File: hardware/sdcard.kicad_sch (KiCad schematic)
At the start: 18 parts

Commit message: train schematics
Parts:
- C?: value 1u -> 4.7u; Voltage 6.3V -> 15V
- C?: Voltage 10V -> 50V
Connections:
- net VDD_SYS_3V3 renamed VDD_AUX_3V3
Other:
- company: Erdapfel -> Frisius
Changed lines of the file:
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@@
     (date "2021-12-17")
     (rev "A")
-    (company "Erdapfel")
+    (company "Frisius")
   )
   (junction (at 109.22 72.39) (diameter 0) (color 0 0 0 0)
@@
       (effects (font (size 0.8 0.8)) (justify left))
     )
-    (property "Value" "1u" (id 1) (at 82.55 45.72 0)
+    (property "Value" "4.7u" (id 1) (at 82.55 45.72 0)
       (effects (font (size 0.8 0.8)) (justify left))
     )
@@
       (effects (font (size 0.8 0.8)) hide)
     )
-    (property "Voltage" "6.3V" (id 4) (at 82.55 46.99 0)
-      (effects (font (size 0.8 0.8)) (justify left))
-    )
-    (pin "1")
-    (pin "2")
+    (property "Voltage" "15V" (id 4) (at 82.55 46.99 0)
+      (effects (font (size 0.8 0.8)) (justify left))
+    )
+    (pin "1")
+    (pin "2")
+  )
+  (symbol (lib_id "bt_power:VDD_AUX_3V3") (at 72.39 40.64 0) (unit 1)
+    (in_bom no) (on_board no)
+    (property "Reference" "U?" (id 0) (at 72.9234 40.64 0)
+      (effects (font (size 1.27 1.27)) hide)
+    )
+    (property "Value" "VDD_AUX_3V3" (id 1) (at 66.04 36.83 0)
+      (effects (font (size 1.27 1.27)) (justify left))
+    )
+    (property "Footprint" "" (id 2) (at 72.9234 40.64 0)
+      (effects (font (size 1.27 1.27)) hide)
+    )
+    (property "Datasheet" "" (id 3) (at 72.9234 40.64 0)
+      (effects (font (size 1.27 1.27)) hide)
+    )
+    (pin "1")
   )
   (symbol (lib_id "Device:R_Small") (at 99.06 45.72 180) (unit 1)
@@
     (pin "2")
   )
-  (symbol (lib_id "bt_power:VDD_SYS_3V3") (at 72.39 40.64 0) (mirror y) (unit 1)
-    (in_bom no) (on_board no)
-    (property "Reference" "U?" (id 0) (at 71.8566 40.64 0)
-      (effects (font (size 0.8 0.8)) hide)
-    )
-    (property "Value" "VDD_SYS_3V3" (id 1) (at 72.39 36.83 0)
-      (effects (font (size 0.8 0.8)))
-    )
-    (property "Footprint" "" (id 2) (at 71.8566 40.64 0)
-      (effects (font (size 0.8 0.8)) hide)
-    )
-    (property "Datasheet" "" (id 3) (at 71.8566 40.64 0)
-      (effects (font (size 0.8 0.8)) hide)
-    )
-    (pin "1")
-  )
   (symbol (lib_id "Device:R_Small") (at 93.98 45.72 180) (unit 1)
     (in_bom yes) (on_board yes)
@@
       (effects (font (size 0.8 0.8)) hide)
     )
-    (property "Voltage" "10V" (id 4) (at 74.93 46.99 0)
-      (effects (font (size 0.8 0.8)) (justify left))
-    )
+    (property "Voltage" "50V" (id 4) (at 74.93 46.99 0)
+      (effects (font (size 0.8 0.8)) (justify left))
+    )

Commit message: ready for first review
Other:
- moved on the sheet: C?, J?, R?

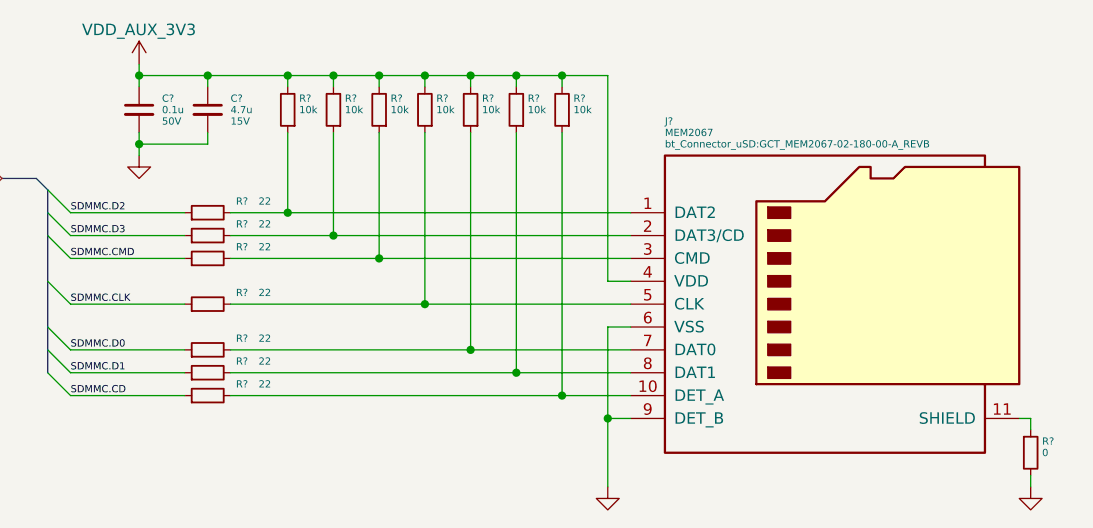
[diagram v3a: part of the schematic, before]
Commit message: checking footprint assignment, added current sense pac1934 for dev
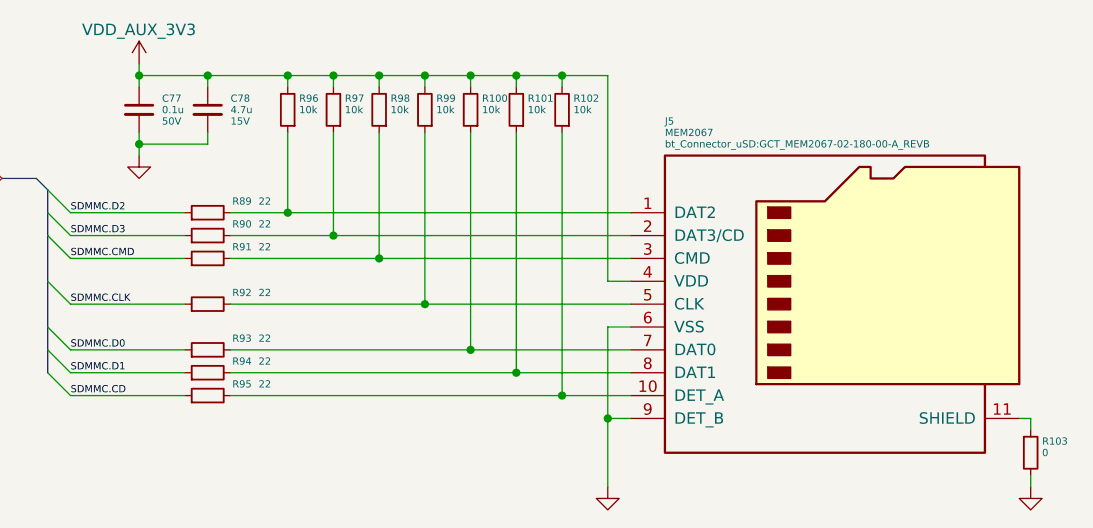
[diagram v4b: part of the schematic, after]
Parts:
- gave numbers to parts that had none: 18
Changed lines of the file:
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@@
   (symbol (lib_id "Device:R_Small") (at 111.76 90.17 90) (unit 1)
     (in_bom yes) (on_board yes)
-    (property "Reference" "R?" (id 0) (at 115.57 88.9 90)
+    (property "Reference" "R89" (id 0) (at 115.57 88.9 90)
       (effects (font (size 0.8 0.8)))
     )
@@
   (symbol (lib_id "Device:R_Small") (at 111.76 110.49 90) (unit 1)
     (in_bom yes) (on_board yes)
-    (property "Reference" "R?" (id 0) (at 115.57 109.22 90)
+    (property "Reference" "R95" (id 0) (at 115.57 109.22 90)
       (effects (font (size 0.8 0.8)))
     )
@@
   (symbol (lib_id "Device:R_Small") (at 120.65 78.74 180) (unit 1)
     (in_bom yes) (on_board yes)
-    (property "Reference" "R?" (id 0) (at 121.92 77.47 0)
+    (property "Reference" "R96" (id 0) (at 121.92 77.47 0)
       (effects (font (size 0.8 0.8)) (justify right))
     )
@@
   (symbol (lib_id "Device:C_Small") (at 111.76 78.74 0) (unit 1)
     (in_bom yes) (on_board yes)
-    (property "Reference" "C?" (id 0) (at 114.3 77.47 0)
+    (property "Reference" "C78" (id 0) (at 114.3 77.47 0)
       (effects (font (size 0.8 0.8)) (justify left))
     )
@@
   (symbol (lib_id "bt_power:VDD_AUX_3V3") (at 104.14 73.66 0) (unit 1)
     (in_bom no) (on_board no)
-    (property "Reference" "U?" (id 0) (at 104.6734 73.66 0)
+    (property "Reference" "#U046" (id 0) (at 104.6734 73.66 0)
       (effects (font (size 1.27 1.27)) hide)
     )
@@
   (symbol (lib_id "Device:R_Small") (at 130.81 78.74 180) (unit 1)
     (in_bom yes) (on_board yes)
-    (property "Reference" "R?" (id 0) (at 132.08 77.47 0)
+    (property "Reference" "R98" (id 0) (at 132.08 77.47 0)
       (effects (font (size 0.8 0.8)) (justify right))
     )
@@
   (symbol (lib_id "Device:R_Small") (at 203.2 116.84 0) (unit 1)
     (in_bom no) (on_board yes)
-    (property "Reference" "R?" (id 0) (at 204.47 115.57 0)
+    (property "Reference" "R103" (id 0) (at 204.47 115.57 0)
       (effects (font (size 0.8 0.8)) (justify left))
     )
@@
   (symbol (lib_id "power:GND") (at 156.21 120.65 0) (unit 1)
     (in_bom yes) (on_board yes)
-    (property "Reference" "#PWR?" (id 0) (at 156.21 127 0)
+    (property "Reference" "#PWR081" (id 0) (at 156.21 127 0)
       (effects (font (size 0.8 0.8)) hide)
     )
@@
   (symbol (lib_id "Device:R_Small") (at 111.76 92.71 90) (unit 1)
     (in_bom yes) (on_board yes)
-    (property "Reference" "R?" (id 0) (at 115.57 91.44 90)
+    (property "Reference" "R90" (id 0) (at 115.57 91.44 90)
       (effects (font (size 0.8 0.8)))
     )
@@
   (symbol (lib_id "Device:R_Small") (at 125.73 78.74 180) (unit 1)
     (in_bom yes) (on_board yes)
-    (property "Reference" "R?" (id 0) (at 127 77.47 0)
+    (property "Reference" "R97" (id 0) (at 127 77.47 0)
       (effects (font (size 0.8 0.8)) (justify right))
     )
@@
   (symbol (lib_id "Device:R_Small") (at 111.76 105.41 90) (unit 1)
     (in_bom yes) (on_board yes)
-    (property "Reference" "R?" (id 0) (at 115.57 104.14 90)
+    (property "Reference" "R93" (id 0) (at 115.57 104.14 90)
       (effects (font (size 0.8 0.8)))
     )
@@
   (symbol (lib_id "Device:R_Small") (at 111.76 95.25 90) (unit 1)
     (in_bom yes) (on_board yes)
-    (property "Reference" "R?" (id 0) (at 115.57 93.98 90)
+    (property "Reference" "R91" (id 0) (at 115.57 93.98 90)
       (effects (font (size 0.8 0.8)))
     )
@@
   (symbol (lib_id "Device:R_Small") (at 146.05 78.74 180) (unit 1)
     (in_bom yes) (on_board yes)
-    (property "Reference" "R?" (id 0) (at 147.32 77.47 0)
+    (property "Reference" "R101" (id 0) (at 147.32 77.47 0)
       (effects (font (size 0.8 0.8)) (justify right))
     )
@@
   (symbol (lib_id "Device:R_Small") (at 111.76 100.33 90) (unit 1)
     (in_bom yes) (on_board yes)
-    (property "Reference" "R?" (id 0) (at 115.57 99.06 90)
+    (property "Reference" "R92" (id 0) (at 115.57 99.06 90)
       (effects (font (size 0.8 0.8)))
     )
@@
   (symbol (lib_id "Device:R_Small") (at 135.89 78.74 180) (unit 1)
     (in_bom yes) (on_board yes)
-    (property "Reference" "R?" (id 0) (at 137.16 77.47 0)
+    (property "Reference" "R99" (id 0) (at 137.16 77.47 0)
       (effects (font (size 0.8 0.8)) (justify right))
     )
@@
   (symbol (lib_id "power:GND") (at 104.14 83.82 0) (mirror y) (unit 1)
     (in_bom yes) (on_board yes)
-    (property "Reference" "#PWR?" (id 0) (at 104.14 90.17 0)
+    (property "Reference" "#PWR080" (id 0) (at 104.14 90.17 0)
       (effects (font (size 0.8 0.8)) hide)
     )
@@
   (symbol (lib_id "Device:R_Small") (at 111.76 107.95 90) (unit 1)
     (in_bom yes) (on_board yes)
-    (property "Reference" "R?" (id 0) (at 115.57 106.68 90)
+    (property "Reference" "R94" (id 0) (at 115.57 106.68 90)
       (effects (font (size 0.8 0.8)))
     )
@@
   (symbol (lib_id "power:GND") (at 203.2 120.65 0) (unit 1)
     (in_bom yes) (on_board yes)
-    (property "Reference" "#PWR?" (id 0) (at 203.2 127 0)
+    (property "Reference" "#PWR082" (id 0) (at 203.2 127 0)
       (effects (font (size 0.8 0.8)) hide)
     )
@@
   (symbol (lib_id "Device:R_Small") (at 140.97 78.74 180) (unit 1)
     (in_bom yes) (on_board yes)
-    (property "Reference" "R?" (id 0) (at 142.24 77.47 0)
+    (property "Reference" "R100" (id 0) (at 142.24 77.47 0)
       (effects (font (size 0.8 0.8)) (justify right))
     )
@@
   (symbol (lib_id "Device:R_Small") (at 151.13 78.74 180) (unit 1)
     (in_bom yes) (on_board yes)
-    (property "Reference" "R?" (id 0) (at 152.4 77.47 0)
+    (property "Reference" "R102" (id 0) (at 152.4 77.47 0)
       (effects (font (size 0.8 0.8)) (justify right))
     )
@@
   (symbol (lib_id "Device:C_Small") (at 104.14 78.74 0) (unit 1)
     (in_bom yes) (on_board yes)
-    (property "Reference" "C?" (id 0) (at 106.68 77.47 0)
+    (property "Reference" "C77" (id 0) (at 106.68 77.47 0)
       (effects (font (size 0.8 0.8)) (justify left))
     )
@@
   (symbol (lib_id "Connector:Micro_SD_Card_Det") (at 181.61 100.33 0) (unit 1)
     (in_bom yes) (on_board yes)
-    (property "Reference" "J?" (id 0) (at 162.56 80.01 0)
-      (effects (font (size 0.8 0.8)) (justify left))
-    )
+    (property "Reference" "J5" (id 0) (at 162.56 80.01 0)
+      (effects (font (size 0.8 0.8)) (justify left))
+    )

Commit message: hardware update
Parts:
- removed R103: 0, Resistor_SMD:R_0603_1608Metric, symbol Device:R_Small
- R45: renamed from R89; footprint Resistor_SMD:R_0603_1608Metric -> Resistor_SMD:R_0402_1005Metric
- R46: renamed from R90; footprint Resistor_SMD:R_0603_1608Metric -> Resistor_SMD:R_0402_1005Metric
- R47: renamed from R91; footprint Resistor_SMD:R_0603_1608Metric -> Resistor_SMD:R_0402_1005Metric
- R48: renamed from R92; footprint Resistor_SMD:R_0603_1608Metric -> Resistor_SMD:R_0402_1005Metric
- R49: renamed from R93; footprint Resistor_SMD:R_0603_1608Metric -> Resistor_SMD:R_0402_1005Metric
- R50: renamed from R94; footprint Resistor_SMD:R_0603_1608Metric -> Resistor_SMD:R_0402_1005Metric
- R51: renamed from R95; footprint Resistor_SMD:R_0603_1608Metric -> Resistor_SMD:R_0402_1005Metric
- R52: renamed from R96; footprint Resistor_SMD:R_0603_1608Metric -> Resistor_SMD:R_0402_1005Metric
- R53: renamed from R97; footprint Resistor_SMD:R_0603_1608Metric -> Resistor_SMD:R_0402_1005Metric
- R54: renamed from R98; footprint Resistor_SMD:R_0603_1608Metric -> Resistor_SMD:R_0402_1005Metric
- R55: renamed from R99; footprint Resistor_SMD:R_0603_1608Metric -> Resistor_SMD:R_0402_1005Metric
- R56: renamed from R100; footprint Resistor_SMD:R_0603_1608Metric -> Resistor_SMD:R_0402_1005Metric
- R57: renamed from R101; footprint Resistor_SMD:R_0603_1608Metric -> Resistor_SMD:R_0402_1005Metric
- R58: renamed from R102; footprint Resistor_SMD:R_0603_1608Metric -> Resistor_SMD:R_0402_1005Metric
- renumbered C77 to C53, C78 to C54, J5 to J4
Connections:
- net GND: now also J4.11 (SHIELD)

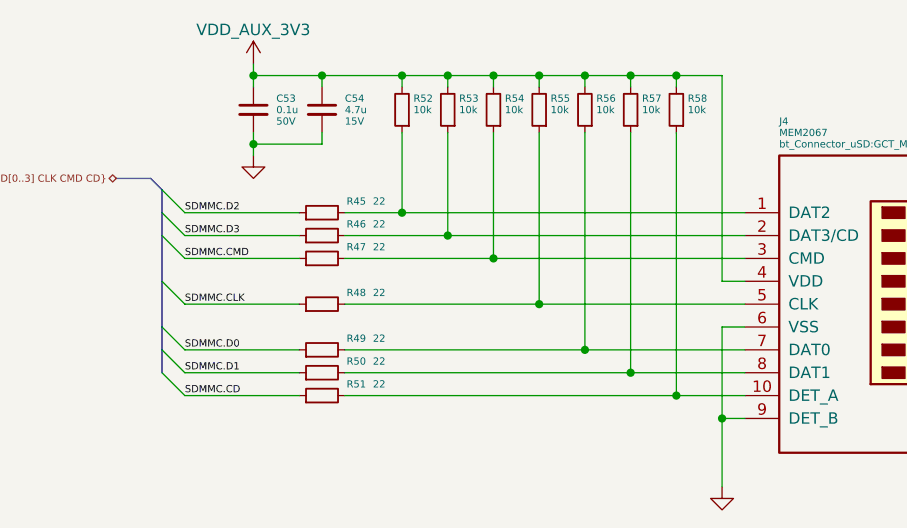
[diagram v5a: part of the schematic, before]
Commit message: initial component placement and design simplification
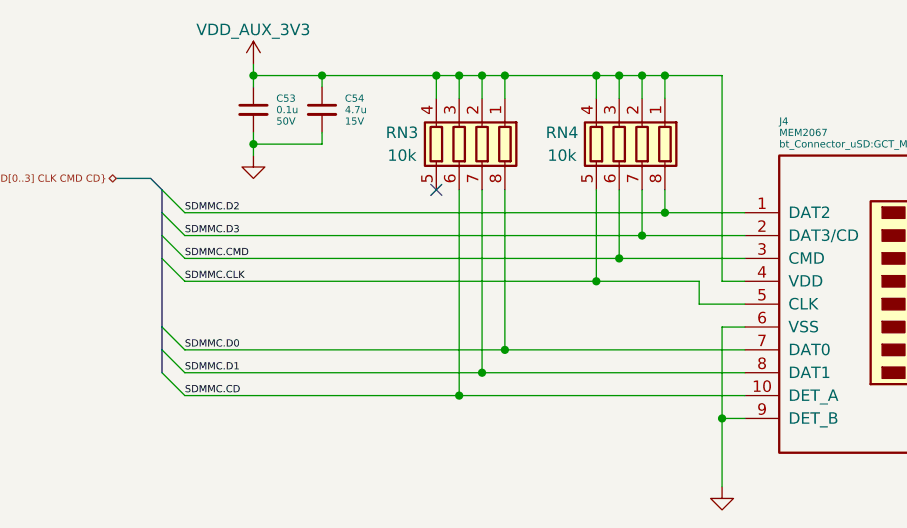
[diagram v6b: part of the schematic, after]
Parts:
- removed R45, R46, R47, R48, R49, R50, R51: 22, Resistor_SMD:R_0402_1005Metric, symbol Device:R_Small
- removed R52, R53, R54, R55, R56, R57, R58: 10k, Resistor_SMD:R_0402_1005Metric, symbol Device:R_Small
- added RN3, RN4: 10k, Resistor_SMD:R_Array_Concave_4x0402, symbol Device:R_Pack04
- C53: footprint Capacitor_SMD:C_0603_1608Metric -> Capacitor_SMD:C_0402_1005Metric
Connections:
- net SDMMC.CD: now also J4.10 (DET_A), RN3.6 (R3.2)
- net SDMMC.CLK: now also J4.5 (CLK), RN4.5 (R4.2)
- net SDMMC.CMD: now also J4.3 (CMD), RN4.6 (R3.2)
- net SDMMC.D0: now also J4.7 (DAT0), RN3.8 (R1.2)
- net SDMMC.D1: now also J4.8 (DAT1), RN3.7 (R2.2)
- net SDMMC.D2: now also J4.1 (DAT2), RN4.8 (R1.2)
- net SDMMC.D3: now also J4.2 (DAT3/CD), RN4.7 (R2.2)
- net VDD_AUX_3V3: now also RN3.1 (R1.1), RN3.2 (R2.1), RN3.3 (R3.1), RN3.4 (R4.1), RN4.1 (R1.1), RN4.2 (R2.1), RN4.3 (R3.1), RN4.4 (R4.1)
- no-connect marks 0 -> 1

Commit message: fixing submodule
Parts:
- removed RN3, RN4: 10k, Resistor_SMD:R_Array_Concave_4x0402, symbol Device:R_Pack04
- added R32, R33, R34, R35, R41, R42: 22, Resistor_SMD:R_0402_1005Metric, symbol Device:R_Small
- added R44, R45, R46, R47, R48, R49: 10k, Resistor_SMD:R_0402_1005Metric, symbol Device:R_Small
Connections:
- net SDMMC.CD is gone; now on net GND: J4.10 (DET_A)
- net SDMMC.CLK: now also R35.1; no longer J4.5 (CLK)
- net SDMMC.CMD: now also R34.1; no longer J4.3 (CMD)
- net SDMMC.D0: now also R41.1; no longer J4.7 (DAT0)
- net SDMMC.D1: now also R42.1; no longer J4.8 (DAT1)
- net SDMMC.D2: now also R32.1; no longer J4.1 (DAT2)
- net SDMMC.D3: now also R33.1; no longer J4.2 (DAT3/CD)
- net VDD_AUX_3V3: now also R44.1, R45.1, R46.1, R47.1, R48.1, R49.1
- new net: J4.1 (DAT2), R32.2, R44.2
- new net: J4.8 (DAT1), R42.2, R49.2
- new net: J4.2 (DAT3/CD), R33.2, R45.2
- new net: J4.7 (DAT0), R41.2, R48.2
- new net: J4.3 (CMD), R34.2, R46.2
- new net: J4.5 (CLK), R35.2, R47.2
- no-connect marks 1 -> 0
